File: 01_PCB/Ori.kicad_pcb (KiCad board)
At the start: 2 copper layers, 277.4 x 75.8 mm, 168 parts, among them J1 TYPE-C-31-M12_13, J2 AVR-ISP-6_mod, K1 KEYSW, K10 KEYSW, K11 KEYSW, K12 KEYSW, K13 KEYSW, K14 KEYSW, K15 KEYSW, K16 KEYSW, K17 KEYSW, K18 KEYSW, K19 KEYSW, K2 KEYSW, K20 KEYSW, K21 KEYSW, K22 KEYSW, K23 KEYSW, K24 KEYSW, K25 KEYSW, K26 KEYSW, K27 KEYSW, K28 KEYSW, K29 KEYSW, K3 KEYSW, K30 KEYSW, K31 KEYSW, K32 KEYSW, K33 KEYSW, K34 KEYSW, K35 KEYSW, K36 KEYSW, K37 KEYSW, K38 KEYSW, K39 KEYSW, K4 KEYSW, K40 KEYSW, K41 KEYSW, K42 KEYSW, K43 KEYSW, K44 KEYSW, K45 KEYSW, K46 KEYSW, K47 KEYSW, K48 KEYSW, K5 KEYSW, K51 KEYSW, K52 KEYSW, K55 KEYSW, K56 KEYSW, K59 KEYSW, K6 KEYSW, K60 KEYSW, K63 KEYSW, K64 KEYSW, K7 KEYSW, K8 KEYSW, K9 KEYSW, SW1 SW_PUSH, SW2 Rotary_Encoder_Switch, SW3 Rotary_Encoder_Switch, SW4 Rotary_Encoder_Switch, SW5 Rotary_Encoder_Switch, SW6 Rotary_Encoder_Switch, SW7 Rotary_Encoder_Switch, SW8 Rotary_Encoder_Switch, SW9 Rotary_Encoder_Switch, U1 ATMEGA32U4, U3 USBLC6-2SC6, Y1 16MHz

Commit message: remove a column
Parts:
- removed D51, D55, D59, D63: D, Keeb_footprints:D_SOD-123_modified
- removed H7, H9: MountingHole, random-keyboard-parts:Generic-Mounthole
- removed K51, K55, K59, K63: KEYSW, Keeb_footprints:MX100
- removed SW3, SW5, SW6, SW7: Rotary_Encoder_Switch, Keebio-Parts:RotaryEncoder_EC11
- moved H21 225.9 mm to (78.7, 91.2)
- moved H22 225.9 mm to (78.7, 72.2)
- moved SW9 140.7 mm to (61.6, 91.2), turned to 90 degrees
- moved SW8 126.3 mm to (61.6, 72.2), turned to 90 degrees
- moved D52 21.2 mm to (70.0, 49.8), turned to 90 degrees
- moved D64 14.0 mm to (70.0, 106.8), turned to 90 degrees
- moved D60 11.2 mm to (70.0, 85.8), turned to 90 degrees
- moved D56 10.7 mm to (70.0, 68.8), turned to 90 degrees
- moved H19 9.50 mm to (78.7, 53.2)
- moved H20 9.50 mm to (78.7, 110.2)
- moved R5 5.76 mm to (100.5, 48.1), turned to 180 degrees
- moved D8 5.00 mm to (212.2, 55.1), turned to 90 degrees
- moved D9 5.00 mm to (247.0, 55.1), turned to 90 degrees
- moved D10 5.00 mm to (250.2, 55.1), turned to 90 degrees
- moved D7 5.00 mm to (209.1, 55.1), turned to 90 degrees
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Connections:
- SW2 pad A: Enc0a -> enc0a
- SW2 pad B: Enc0b -> enc0b
- SW4 pad A: Enc0a -> enc3a
- SW4 pad B: Enc0b -> enc3b
- SW8 pad A: Enc0a -> enc1a
- SW8 pad B: Enc0b -> enc1b
- SW8 pad S1: Net-(D42-Pad2) -> Net-(D56-Pad2)
- SW8 pad S2: col6 -> col0
- SW9 pad A: Enc1a -> enc2a
- SW9 pad B: Enc1b -> enc2b
- SW9 pad S1: Net-(D43-Pad2) -> Net-(D60-Pad2)
- SW9 pad S2: col7 -> col0
- U1 pad 18: Enc1b -> enc3a
- U1 pad 19: Enc1a -> enc3b
- U1 pad 20: Enc0b -> enc0b
- U1 pad 21: Enc0a -> enc0a
- U1 pad 28: (no net) -> enc2b
- U1 pad 29: (no net) -> enc2a
- U1 pad 30: col13 -> enc1b
- U1 pad 32: (no net) -> enc1a
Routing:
- net Enc1b: track 370.4 -> 0.00 mm, vias 3 -> 0
- net Enc1a: track 365.8 -> 0.00 mm, vias 3 -> 0
- net col13: track 317.3 -> 0.00 mm, vias 4 -> 0
- net Enc0b: track 311.3 -> 0.00 mm, vias 6 -> 0
- net Enc0a: track 299.2 -> 0.00 mm, vias 6 -> 0
- net enc0a: track 0.00 -> 94.1 mm, vias 0 -> 2
- net row2: track 381.2 -> 288.9 mm, vias 6 -> 2
- net enc0b: track 0.00 -> 87.7 mm, vias 0 -> 2
- net enc3a: track 0.00 -> 85.2 mm, vias 0 -> 2
- net enc1a: track 0.00 -> 81.8 mm
- net enc3b: track 0.00 -> 79.5 mm, vias 0 -> 2
- net row0: track 338.5 -> 260.4 mm, vias 4 -> 3
- net row3: track 341.4 -> 268.1 mm, vias 2 -> 0
- net enc2a: track 0.00 -> 65.3 mm, vias 0 -> 1
- net enc1b: track 0.00 -> 64.4 mm
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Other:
- board size 277.4 x 75.8 mm -> 251.9 x 76.8 mm
- board text added: "Ori PCB Revision 1.0 20210415"
- board text removed: "Ori PCB Revision 1.0 2020-07-23"

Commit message: routing tomfoolery
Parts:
- removed the D52 at (70.0, 49.8)
- added D49: D, Keeb_footprints:D_SOD-123_modified, B.Cu at (70.0, 49.8)
- renumbered D56 to D50, D60 to D51, D64 to D52, K52 to K49, K56 to K50, K60 to K51, K64 to K52
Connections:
- J1 pad A8: (no net) -> Net-(J1-PadA8)
- J1 pad B8: (no net) -> Net-(J1-PadB8)
- U1 pad 42: (no net) -> Net-(U1-Pad42)
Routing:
- net GND: track 35.6 -> 140.8 mm, vias 8 -> 33
- net row1: track 282.7 -> 254.4 mm
- net enc1a: track 81.8 -> 59.7 mm
- net col12: track 370.0 -> 365.0 mm
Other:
- outline, holes or cut-outs redrawn
- board text added: "Encoder C"
- board text added: "Encoder D"
- board text added: "Ori PCB Revision 1.0 2021.04.24"
- board text removed: "Ori PCB Revision 1.0 20210415"

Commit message: final touches
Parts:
- moved D18 0.26 mm to (174.2, 74.1)
- moved D41 0.19 mm to (171.0, 112.2)
- moved D17 0.19 mm to (171.1, 74.1)
- moved D30 0.11 mm to (174.2, 93.1)
- moved D43 0.09 mm to (209.0, 112.2)

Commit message: update
added macro column to top plate
re-routed some traces
new previews
removed some ground plane
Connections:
- J2 pad 3: col12 -> col0
- K12 pad 1: col12 -> col0
- K24 pad 1: col12 -> col0
- K36 pad 1: col12 -> col0
- K48 pad 1: col12 -> col0
- K49 pad 1: col0 -> col12
- K50 pad 1: col0 -> col12
- K51 pad 1: col0 -> col12
- K52 pad 1: col0 -> col12
- SW2 pad S2: col0 -> col12
- SW4 pad S2: col0 -> col12
- SW8 pad S2: col0 -> col12
- SW9 pad S2: col0 -> col12
- U1 pad 11: col12 -> col0
- U1 pad 31: col0 -> col12
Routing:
- net col12: track 365.0 -> 136.4 mm
- net col0: track 136.4 -> 365.0 mm
- net GND: track 140.8 -> 76.5 mm, vias 33 -> 14
- net VCC: track 257.0 -> 250.9 mm
- net row1: track 254.4 -> 252.6 mm, vias 2 -> 3
- net Net-(D2-Pad2): track 16.1 -> 14.6 mm, vias 0 -> 1
- net Net-(D15-Pad2): track 7.67 -> 7.43 mm, vias 0 -> 1
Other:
- board text added: "Ori PCB Revision 1.0 2021.04.25"
- board text removed: "Ori PCB Revision 1.0 2021.04.24"

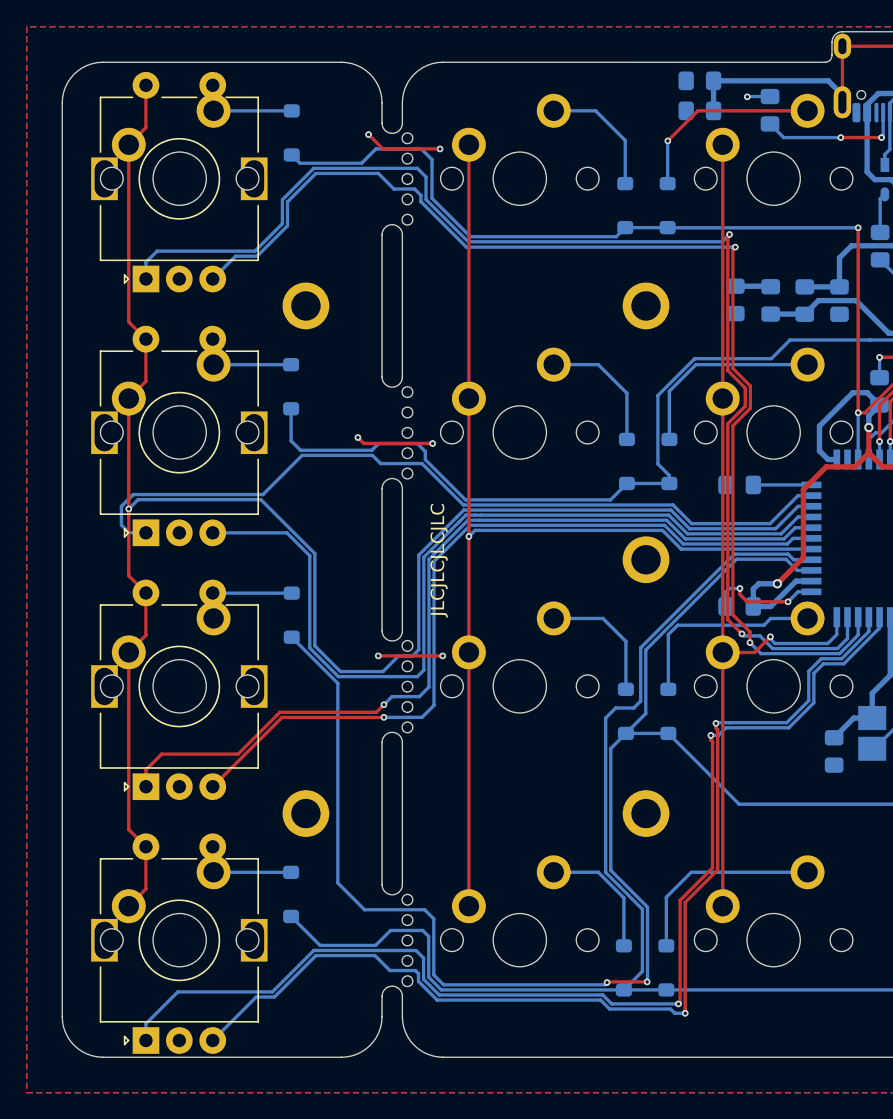
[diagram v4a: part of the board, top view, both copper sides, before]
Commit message: Moved macro column a tiny bit
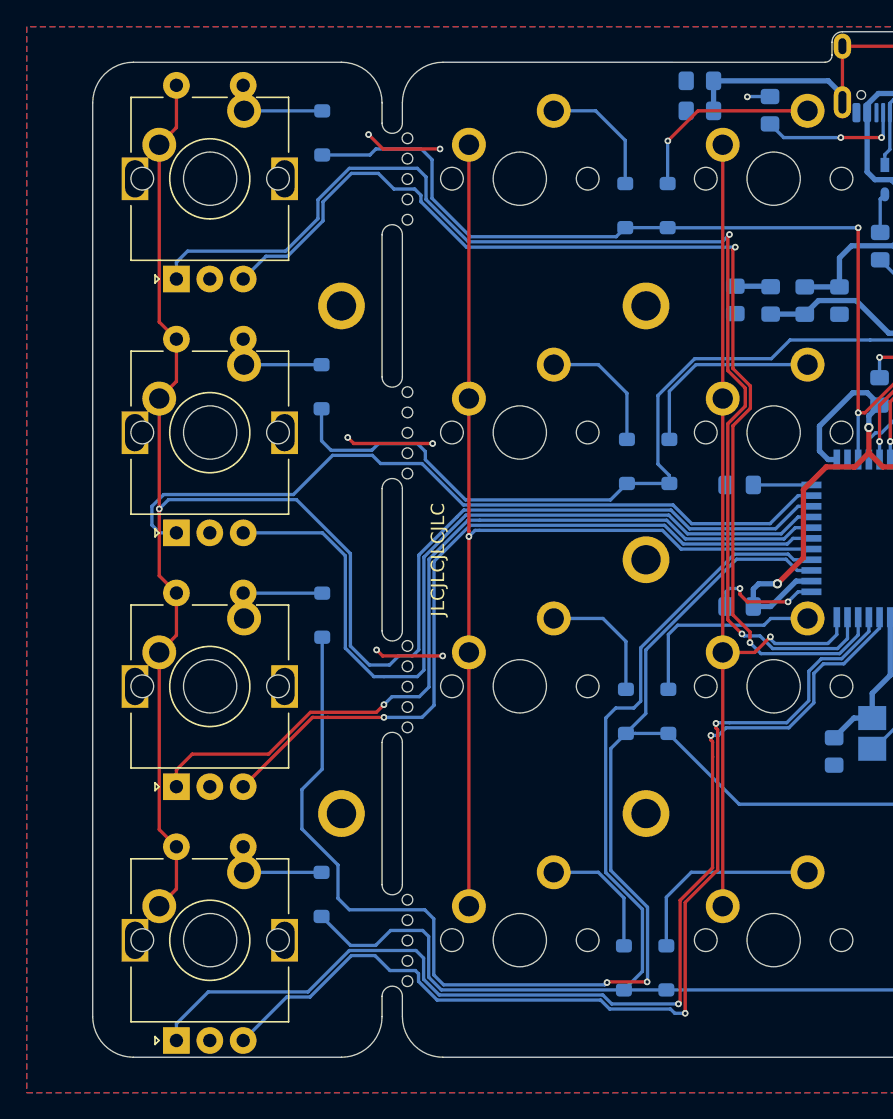
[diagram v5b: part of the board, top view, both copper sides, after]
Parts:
- moved H10 2.66 mm to (73.7, 100.7)
- moved H8 2.66 mm to (73.7, 62.7)
- moved K49 2.28 mm to (63.9, 53.2)
- moved K50 2.28 mm to (63.9, 72.2)
- moved K51 2.28 mm to (63.9, 91.2)
- moved K52 2.28 mm to (63.9, 110.2)
- moved SW2 2.28 mm to (63.9, 53.2)
- moved SW4 2.28 mm to (63.9, 110.2)
- moved SW8 2.28 mm to (63.9, 72.2)
- moved SW9 2.28 mm to (63.9, 91.2)
- moved D49 2.28 mm to (72.3, 49.8)
- moved D50 2.28 mm to (72.2, 68.8)
- moved D51 2.28 mm to (72.3, 85.8)
- moved D52 2.28 mm to (72.2, 106.8)
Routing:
- net row0: track 260.3 -> 257.5 mm
- net col12: track 136.4 -> 133.7 mm
- net enc0a: track 94.1 -> 91.6 mm
- net enc0b: track 87.7 -> 85.2 mm
- net enc2a: track 65.3 -> 63.1 mm
- net row3: track 268.1 -> 265.8 mm
- net row1: track 252.6 -> 250.3 mm
- net enc3b: track 79.5 -> 77.3 mm
- net enc3a: track 85.2 -> 83.0 mm
- net enc2b: track 60.0 -> 57.7 mm
- net enc1a: track 59.7 -> 57.4 mm
- net enc1b: track 64.4 -> 62.1 mm
- net GND: track 76.5 -> 77.6 mm
- net row2: track 288.9 -> 289.9 mm
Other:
- board size 251.9 x 76.8 mm -> 249.7 x 76.8 mm
